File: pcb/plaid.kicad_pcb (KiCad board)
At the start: 2 copper layers, 217.5 x 92.1 mm, 134 parts, among them J2 AVR_ISP_6, J3 Conn_01x04, SW1 SW_Push, SW10 SW_Push, SW11 SW_Push, SW12 SW_Push, SW13 SW_Push, SW14 SW_Push, SW15 SW_Push, SW16 SW_Push, SW17 SW_Push, SW18 SW_Push, SW19 SW_Push, SW2 SW_Push, SW20 SW_Push, SW21 SW_Push, SW22 SW_Push, SW23 SW_Push, SW24 SW_Push, SW25 SW_Push, SW26 SW_Push, SW27 SW_Push, SW28 SW_Push, SW29 SW_Push, SW3 SW_Push, SW30 SW_Push, SW31 SW_Push, SW32 SW_Push, SW33 SW_Push, SW34 SW_Push, SW35 SW_Push, SW36 SW_Push, SW37 SW_Push, SW38 SW_Push, SW39 SW_Push, SW4 SW_Push, SW40 SW_Push, SW41 SW_Push, SW42 SW_Push, SW43 SW_Push, SW44 SW_Push, SW45 SW_Push, SW46 SW_Push, SW47 SW_Push, SW48 SW_Push, SW49 SW_Push, SW5 SW_Push, SW50 RESET, SW51 BOOT, SW6 SW_Push, SW7 SW_Push, SW8 SW_Push, SW9 SW_Push, U1 ATMEGA328-PU, Y1 16MHz

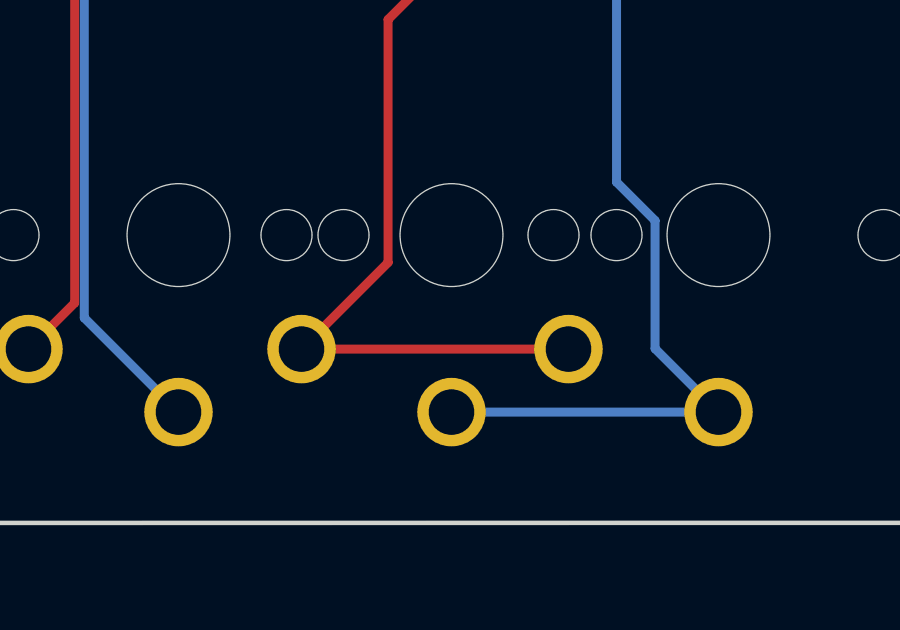
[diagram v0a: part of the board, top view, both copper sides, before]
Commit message: properly align the 2x thumb on bottom row
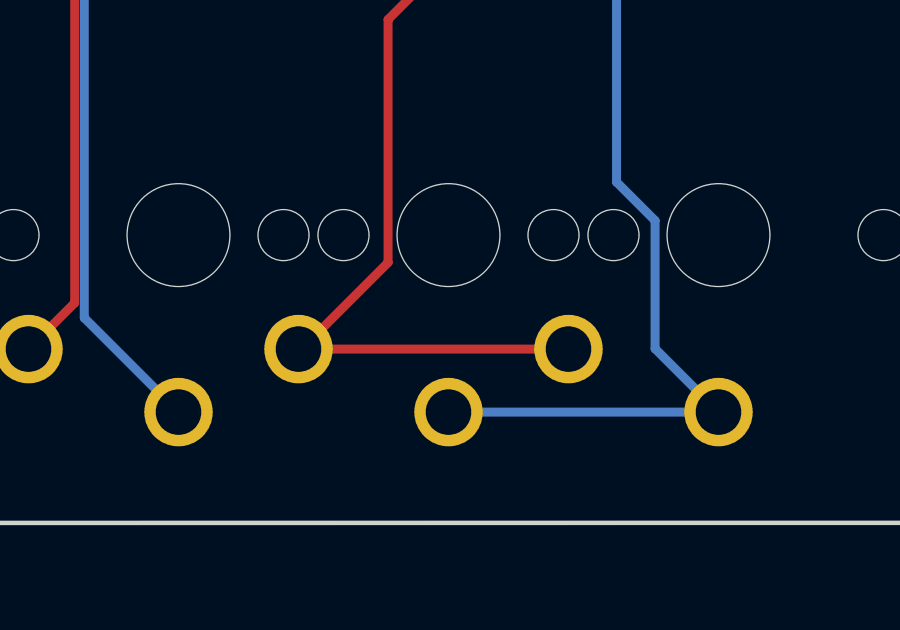
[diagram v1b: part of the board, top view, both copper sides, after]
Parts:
- moved SW49 0.10 mm to (134.0, 135.2)
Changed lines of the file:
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@@
   )
   (footprint "kbd:choc-v1-with-millmax_edit" (layer "F.Cu")
-    (at 134.074 135.2305)
+    (at 133.974 135.2305)
     (descr "Kailh \"Choc\" PG1350 keyswitch, able to be mounted on front or back of PCB")
     (tags "kailh,choc")

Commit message: Actually properly align and place the thumb 2x switch
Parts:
- moved SW49 18.0 mm to (152.0, 135.2)
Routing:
- net /COL6: track 133.4 -> 145.2 mm
- net Net-(D43-Pad2): track 108.4 -> 113.0 mm
- net /COL5: track 139.9 -> 138.5 mm
